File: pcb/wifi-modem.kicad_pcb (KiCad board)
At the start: 4 copper layers, 69 x 67 mm, 55 parts, among them J1 USB_B, J2 Conn_01x03, J3 RS232 DB9, Q1 Q_NPN_BEC, Q2 Q_NPN_BEC, SW1 SW_Push, U1 ESP-12F, U2 74HC245, U3 LM1117-3.3, U4 FT232RL, U5 MAX232

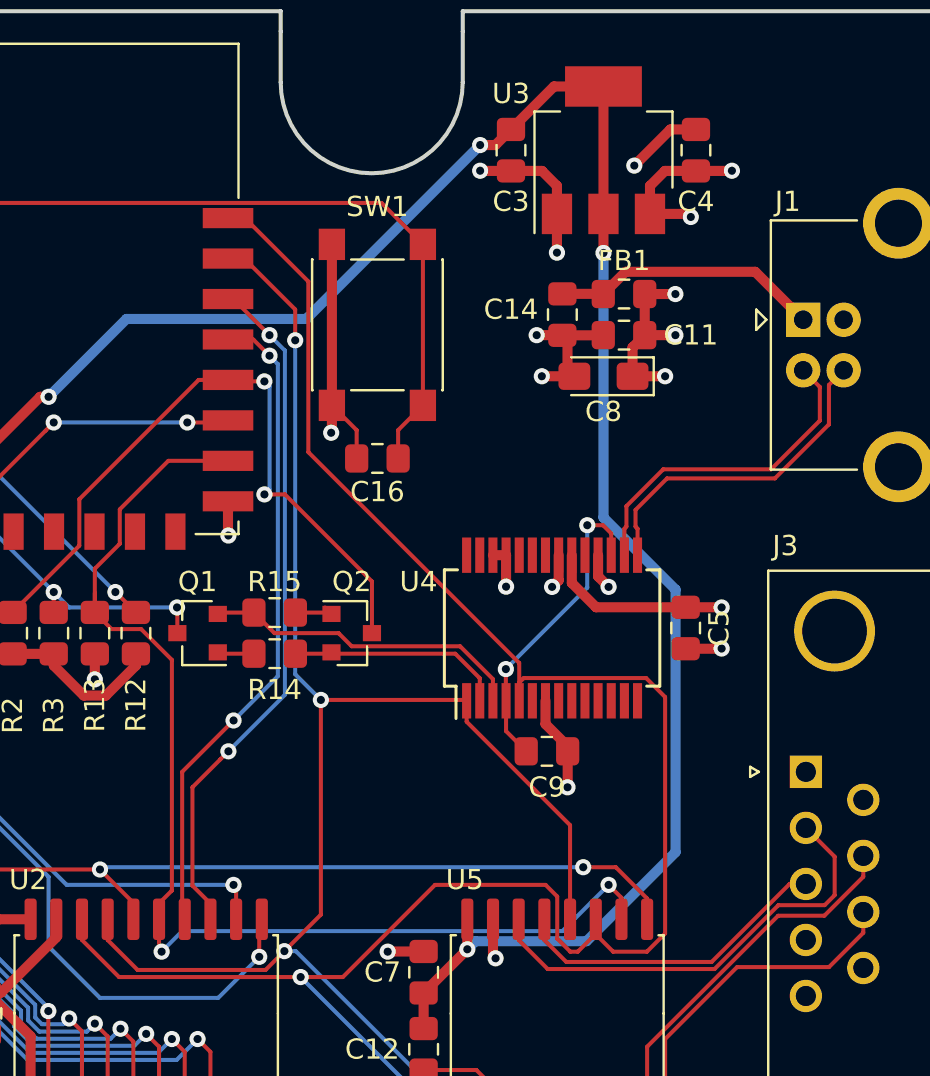
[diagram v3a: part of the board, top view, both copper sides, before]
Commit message: Rotating VBUS filter
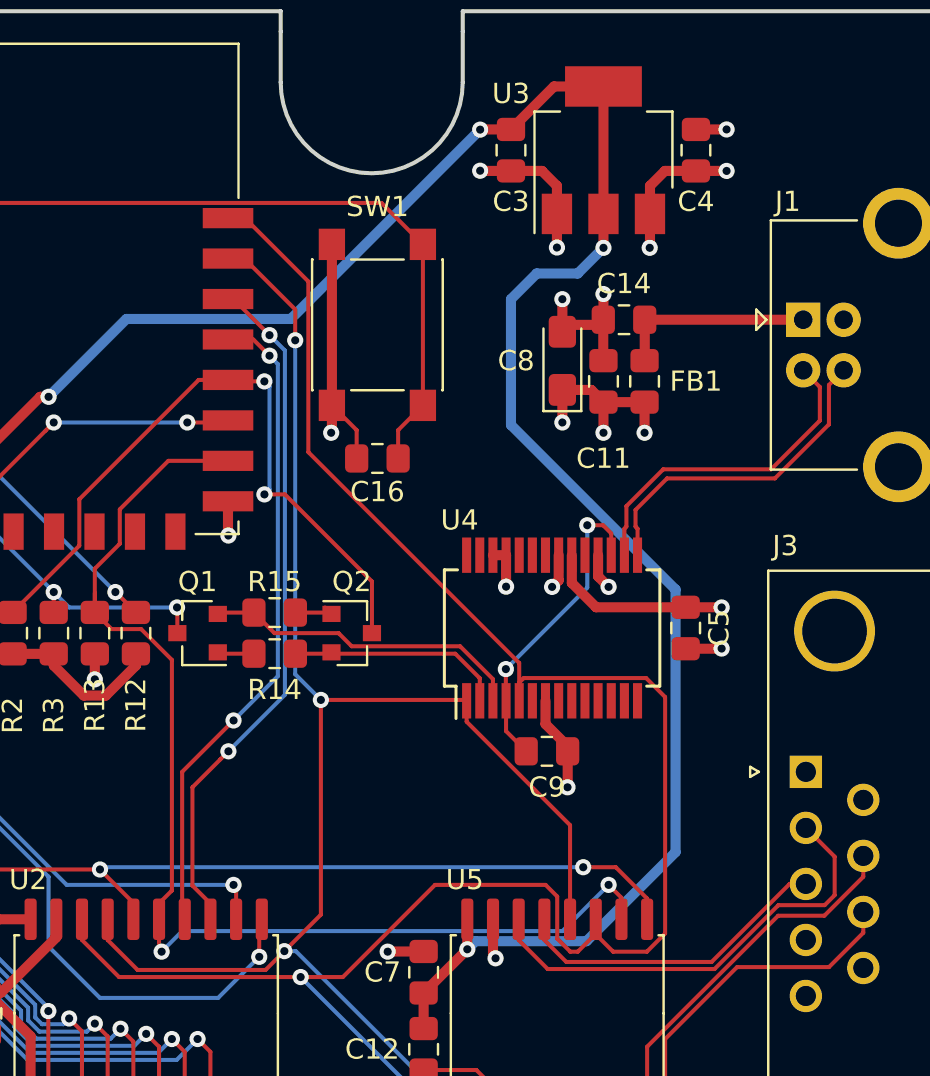
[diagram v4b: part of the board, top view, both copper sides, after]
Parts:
- moved FB1 4.44 mm to (86.6, 81.0), turned to 270 degrees
- moved C14 3.06 mm to (85.6, 78.0), turned to 180 degrees
- moved C11 2.50 mm to (84.6, 81.0), turned to 90 degrees
- moved C8 2.17 mm to (82.5, 80.0), turned to 90 degrees
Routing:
- net +3V3: track 121.3 -> 126.3 mm
- net VBUS: track 13.3 -> 9.86 mm
- net GND: track 82.1 -> 79.6 mm
- net +5V: track 37.4 -> 36.7 mm

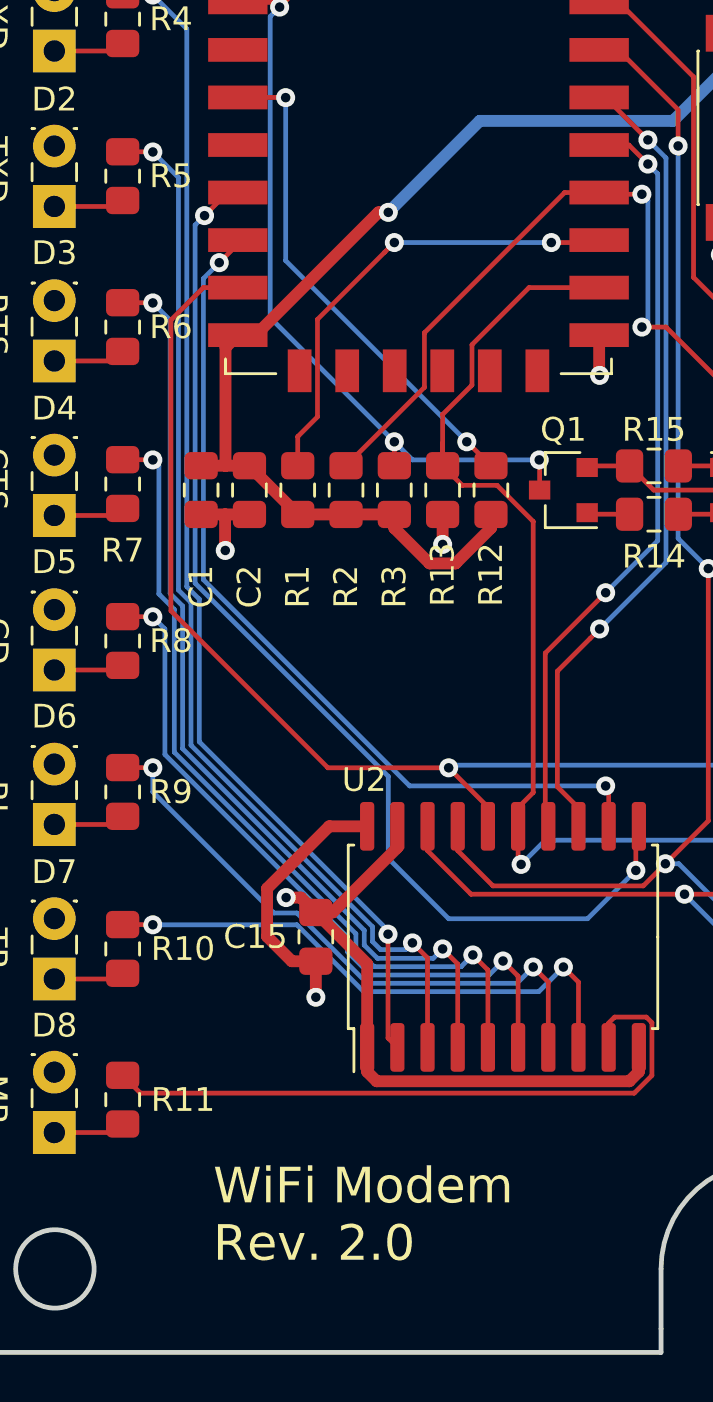
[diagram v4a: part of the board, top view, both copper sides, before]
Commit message: Added transceiver control
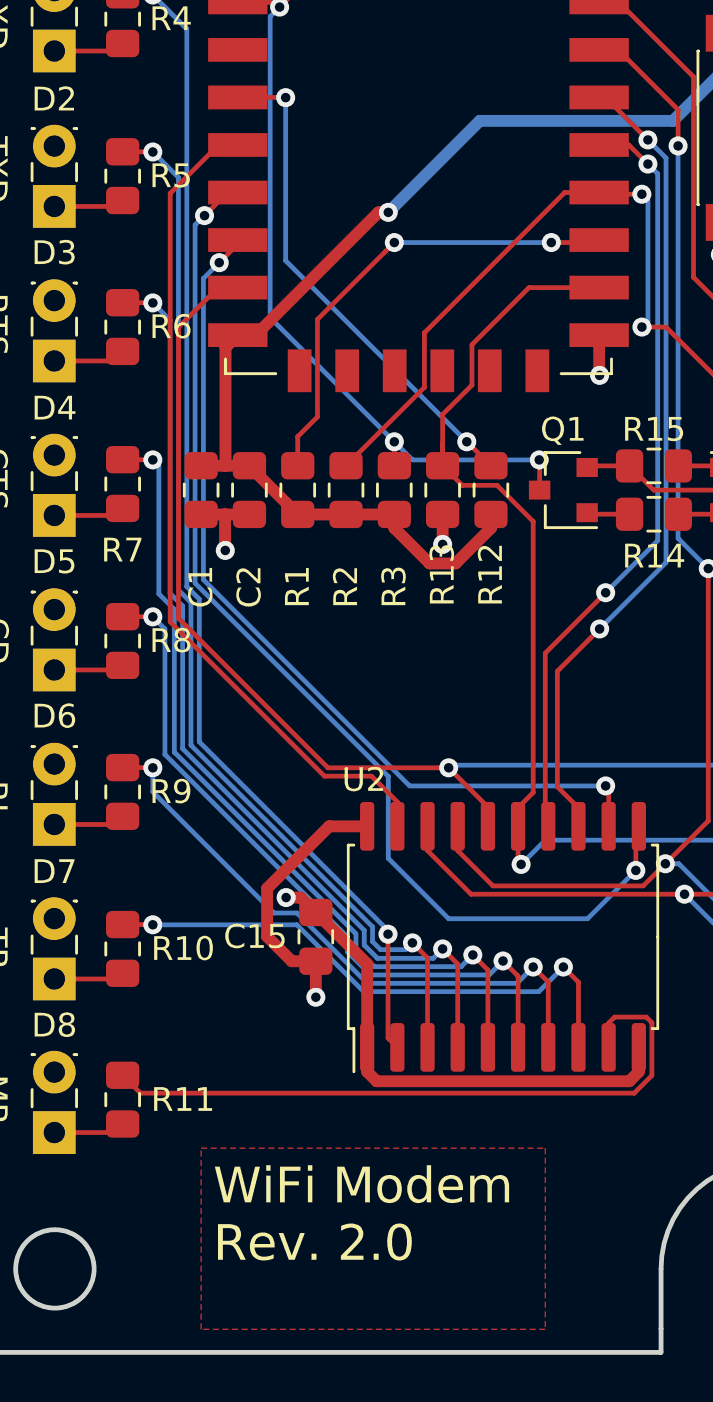
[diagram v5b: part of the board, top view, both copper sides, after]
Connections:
- U1 pad 4: (no net) -> ESP_GPIO16_LED_EN
- U2 pad 19: GND -> ESP_GPIO16_LED_EN
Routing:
- net ESP_GPIO16_LED_EN: track 0.00 -> 35.4 mm
- net GND: track 79.6 -> 74.1 mm
- net ESP_UART0_CTS: track 61.9 -> 61.3 mm
- added copper zone on F.Cu, net (none)

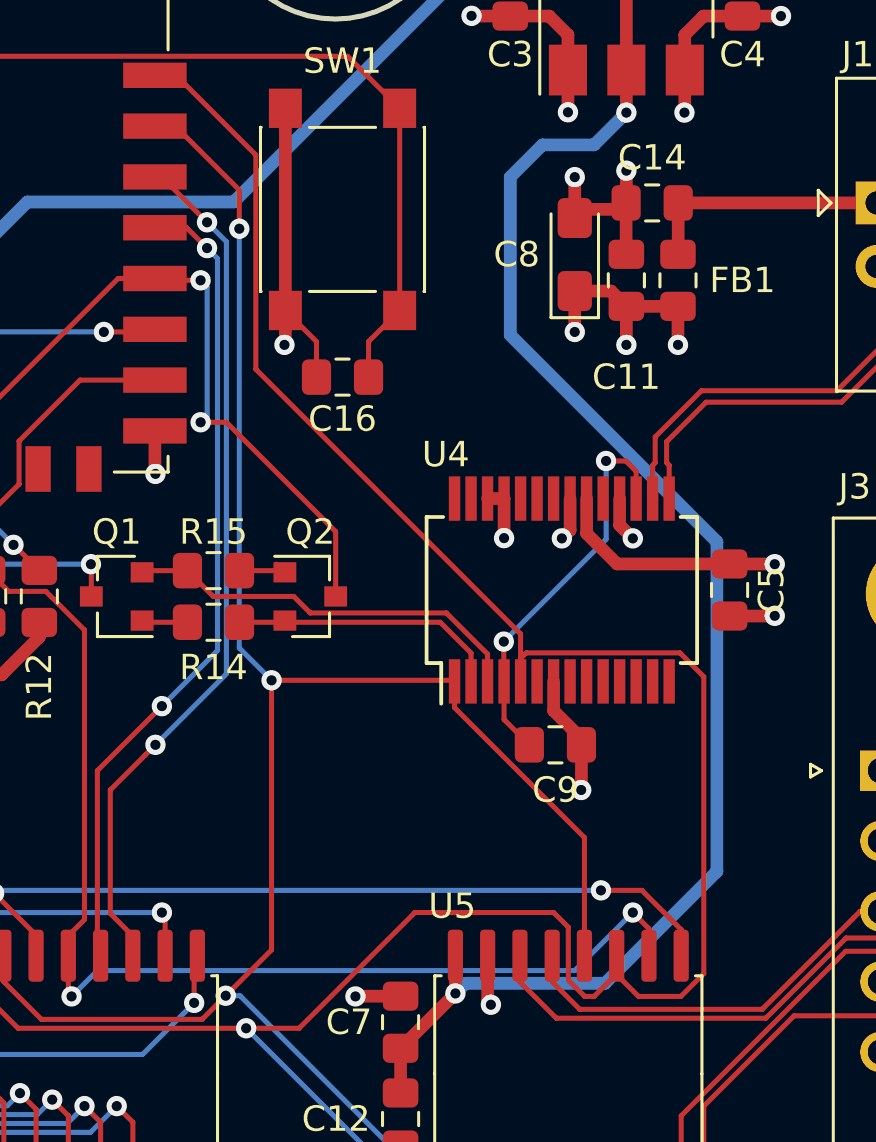
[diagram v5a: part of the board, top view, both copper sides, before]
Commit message: Changing VCCIO supply to external 3V3 LDO
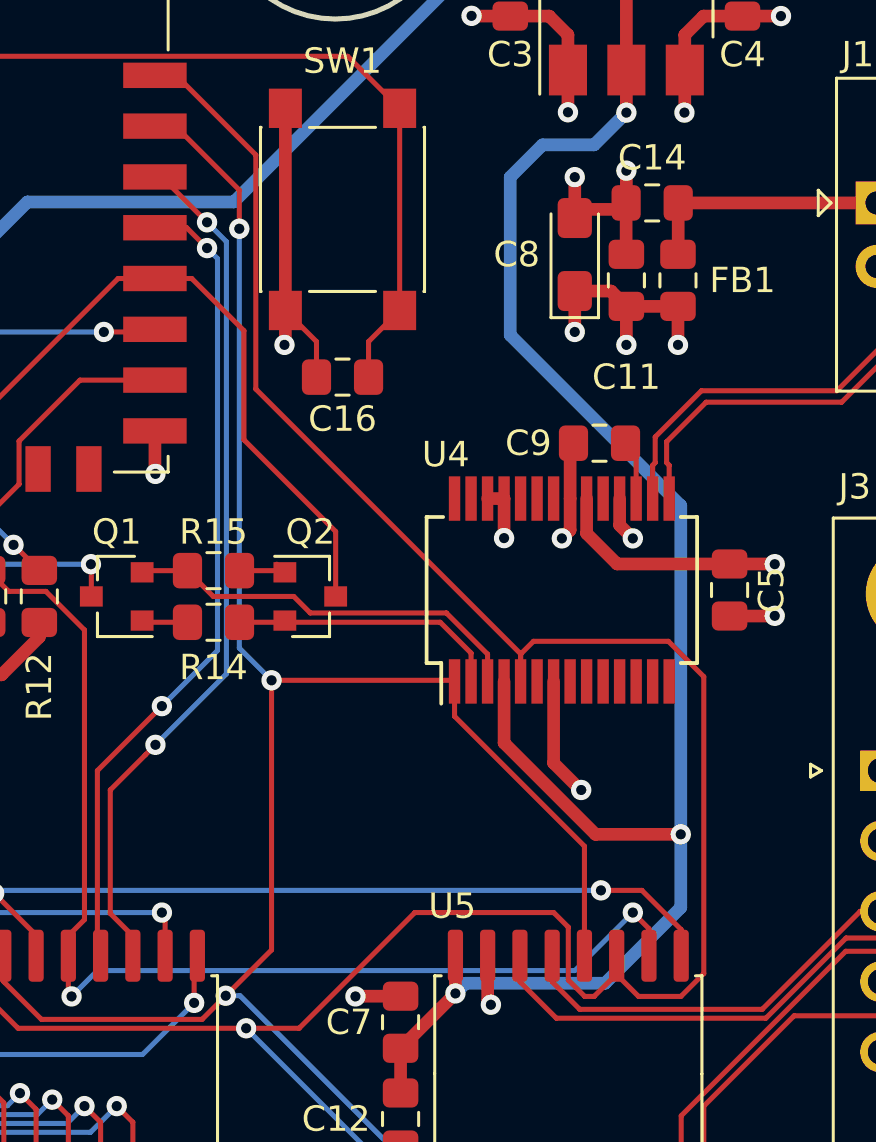
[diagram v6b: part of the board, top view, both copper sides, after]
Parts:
- moved C9 12.0 mm to (83.5, 87.4), turned to 180 degrees
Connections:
- U4 pad 4: FT232_3V3 -> +3V3
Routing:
- net FT232_3V3: track 15.7 -> 2.35 mm, vias 2 -> 0
- net +3V3: track 126.3 -> 136.0 mm, vias 4 -> 5
- net GND: track 74.1 -> 76.3 mm
- net ESP_GPIO0: track 34.0 -> 33.2 mm, vias 2 -> 0

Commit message: Rev 2.1 updates
* Added 3-input AND to handle 3x serial inputs
* Added manual UART BL mode jumper
* Changed footprint of 2 transistors
* Updated refdes of caps
* Using 3V3 LDO for FT232RL IO
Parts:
- added C17: 100n, Capacitor_SMD:C_0805_2012Metric_Pad1.15x1.40mm_HandSolder, F.Cu at (76.5, 154.9)
- added JP1: Jumper_NO_Small, Connector_PinHeader_2.54mm:PinHeader_1x02_P2.54mm_Vertical, F.Cu at (70.5, 66.8)
- added R16: 10k, Resistor_SMD:R_0805_2012Metric_Pad1.15x1.40mm_HandSolder, F.Cu at (84.8, 102.0)
- added U6: 74LVC1G11, Package_TO_SOT_SMD:SOT-23-6_Handsoldering, F.Cu at (81.0, 102.0)
- C13: value 100n -> 4.7u; footprint Capacitor_SMD:C_0805_2012Metric_Pad1.15x1.40mm_HandSolder -> Capacitor_Tantalum_SMD:CP_EIA-3216-18_Kemet-A_Pad1.58x1.35mm_HandSolder
- C14: value 10n -> 100n
- C15: value 100n -> 10n
- C8: value 4.7u -> 100n; footprint Capacitor_Tantalum_SMD:CP_EIA-3216-18_Kemet-A_Pad1.58x1.35mm_HandSolder -> Capacitor_SMD:C_0805_2012Metric_Pad1.15x1.40mm_HandSolder
- Q1, Q2: footprint Package_TO_SOT_SMD:SOT-23 -> Package_TO_SOT_SMD:SOT-23_Handsoldering
- moved C8 70.1 mm to (71.8, 149.2), turned to 0 degrees
- moved C14 68.2 mm to (82.5, 146.1), turned to 0 degrees
- moved C16 64.7 mm to (81.2, 149.1), turned to 0 degrees
- moved C5 60.1 mm to (67.0, 149.2), turned to 0 degrees
- moved C9 58.9 mm to (77.8, 146.1), turned to 0 degrees
- moved C15 45.6 mm to (76.5, 152.0), turned to 0 degrees
- moved C7 42.9 mm to (67.0, 152.2), turned to 0 degrees
- moved C12 35.0 mm to (76.5, 149.1), turned to 0 degrees
- moved C10 34.2 mm to (71.8, 152.2)
- moved C13 32.3 mm to (67.7, 146.2)
- moved C6 27.0 mm to (73.0, 146.1)
- moved Q1 5.27 mm to (69.5, 91.8), turned to 0 degrees
- moved R14 4.93 mm to (63.5, 93.5), turned to 270 degrees
- moved Q2 3.18 mm to (69.5, 95.2)
- moved R15 3.01 mm to (65.5, 93.5), turned to 90 degrees
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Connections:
- C10 pad 1: Net-(C10-Pad1) -> +3V3
- C10 pad 2: Net-(C10-Pad2) -> GND
- C11 pad 1: +5V -> +3V3
- C11 pad 2: GND -> Net-(C11-Pad2)
- C12 pad 1: +3V3 -> Net-(C12-Pad1)
- C12 pad 2: Net-(C12-Pad2) -> GND
- C13 pad 1: Net-(C13-Pad1) -> +5V
- C14 pad 1: VBUS -> +5V
- C15 pad 1: +5V -> VBUS
- C16 pad 1: ESP_RST_N -> +5V
- C5 pad 1: +5V -> +3V3
- C6 pad 1: Net-(C6-Pad1) -> +5V
- C6 pad 2: Net-(C6-Pad2) -> GND
- C7 pad 1: +3V3 -> FT232_3V3
- C8 pad 1: +5V -> Net-(C8-Pad1)
- C8 pad 2: GND -> Net-(C8-Pad2)
- C9 pad 1: FT232_3V3 -> Net-(C9-Pad1)
- C9 pad 2: GND -> Net-(C9-Pad2)
- J2 pad 2: 3V3_TTL_RXD -> 3V3_TTL_HDR_RXD
- U1 pad 21: 3V3_TTL_RXD -> ESP_UART0_RXD
- U2 pad 17: 3V3_TTL_RXD -> ESP_UART0_RXD
- U4 pad 1: 3V3_TTL_RXD -> FT232_TXD
- U5 pad 1: Net-(C6-Pad1) -> Net-(C8-Pad1)
- U5 pad 12: 3V3_TTL_RXD -> MAX232_RXD
- U5 pad 2: Net-(C12-Pad2) -> Net-(C11-Pad2)
- U5 pad 3: Net-(C6-Pad2) -> Net-(C8-Pad2)
- U5 pad 4: Net-(C10-Pad1) -> Net-(C9-Pad1)
- U5 pad 5: Net-(C10-Pad2) -> Net-(C9-Pad2)
- U5 pad 6: Net-(C13-Pad1) -> Net-(C12-Pad1)
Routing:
- net +3V3: track 136.0 -> 0.00 mm, vias 5 -> 0
- net 3V3_TTL_RXD: track 92.4 -> 0.00 mm, vias 3 -> 0
- net ESP_RST_N: track 66.6 -> 0.00 mm, vias 3 -> 0
- net GND: track 76.3 -> 13.9 mm, vias 18 -> 5
- net ESP_GPIO15_UART0_RTS: track 57.9 -> 0.00 mm, vias 2 -> 0
- net ESP_GPIO5: track 34.2 -> 0.00 mm, vias 2 -> 0
- net ESP_GPIO4: track 32.4 -> 0.00 mm, vias 2 -> 0
- net +5V: track 36.7 -> 7.16 mm, vias 7 -> 2
- net ESP_EN: track 21.1 -> 0.00 mm, vias 2 -> 0
- net ESP_GPIO0: track 33.2 -> 16.9 mm
- net FT232_RTS: track 16.1 -> 0.00 mm
- net FT232_DTR: track 11.1 -> 0.00 mm
- net Net-(C12-Pad2): track 4.79 -> 0.00 mm
- net Net-(C6-Pad2): track 3.08 -> 0.00 mm
- net Net-(C13-Pad1): track 3.08 -> 0.00 mm
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
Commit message: Saving work
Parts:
- removed C11: 100n, Capacitor_SMD:C_0805_2012Metric_Pad1.15x1.40mm_HandSolder
- moved JP1 26.0 mm to (96.5, 67.0), turned to 270 degrees
- moved FB1 4.47 mm to (89.9, 78.0), turned to 180 degrees
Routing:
- net +5V: track 7.16 -> 93.4 mm, vias 2 -> 1
- net +3V3: track 0.00 -> 11.8 mm
- net VBUS: track 9.86 -> 3.54 mm
- added copper zone on B.Cu, net GND
- added copper zone on F.Cu, net GND
- removed copper zone on F.Cu, net (none)
- removed copper zone on In2.Cu, net +5V
- removed copper zone on In1.Cu, net GND
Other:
- copper layers 4 -> 2
